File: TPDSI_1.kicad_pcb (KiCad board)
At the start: 2 copper layers, 83.8 x 61 mm, 63 parts, among them J1 Conn_01x02_Male, J2 Conn_01x02_Male, J3 Conn_01x10_Male, J4 Conn_01x04_Male, J5 Conn_01x04_Male, J6 Conn_01x06_Male, J7 Screw_Terminal_01x02, Q1 Q_NPN_BCE, Q2 Q_NPN_BCE, SW1 SW_Push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

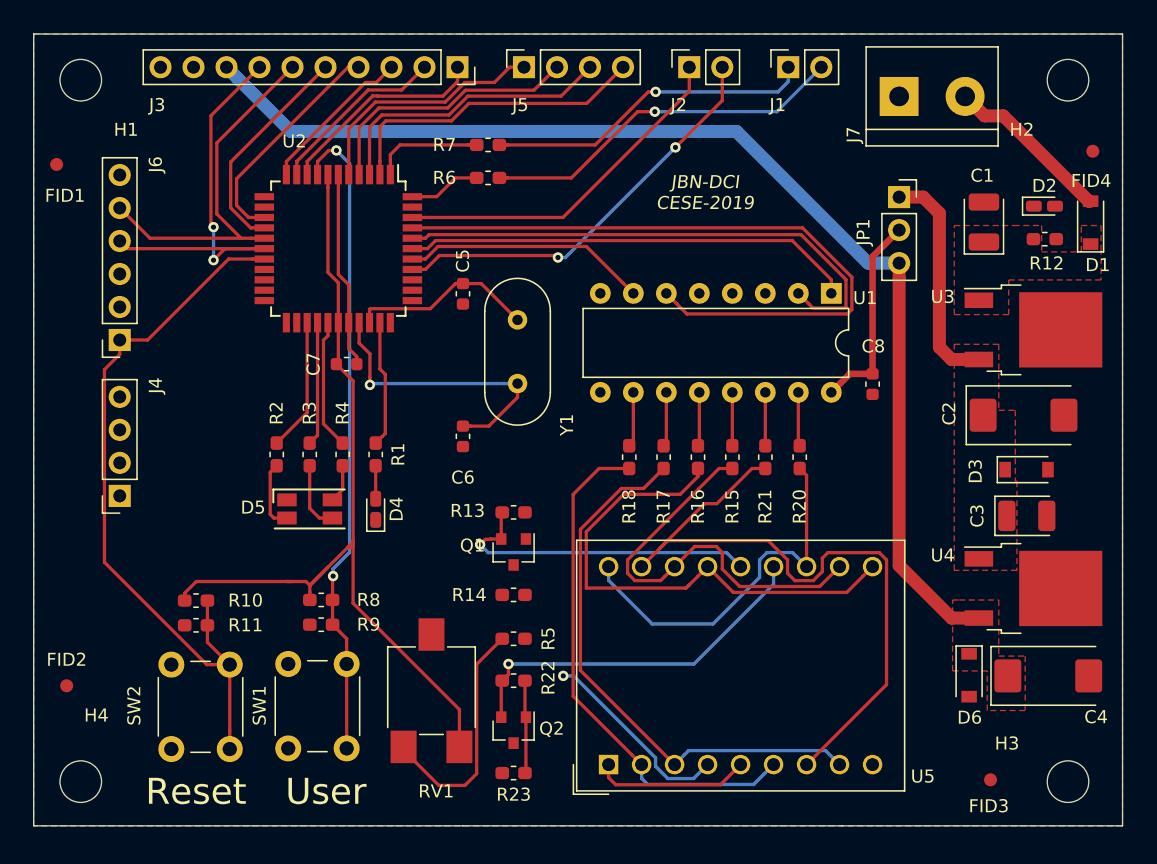
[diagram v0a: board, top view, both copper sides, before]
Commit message: Se agrega terminación de ruteo, con poligono de vcc y planos en top y bottom de gnd, pendiente realizar vías entre planos gnd, agregar datasheet y numeros de parte , insertar 3modelos  3D faltantes
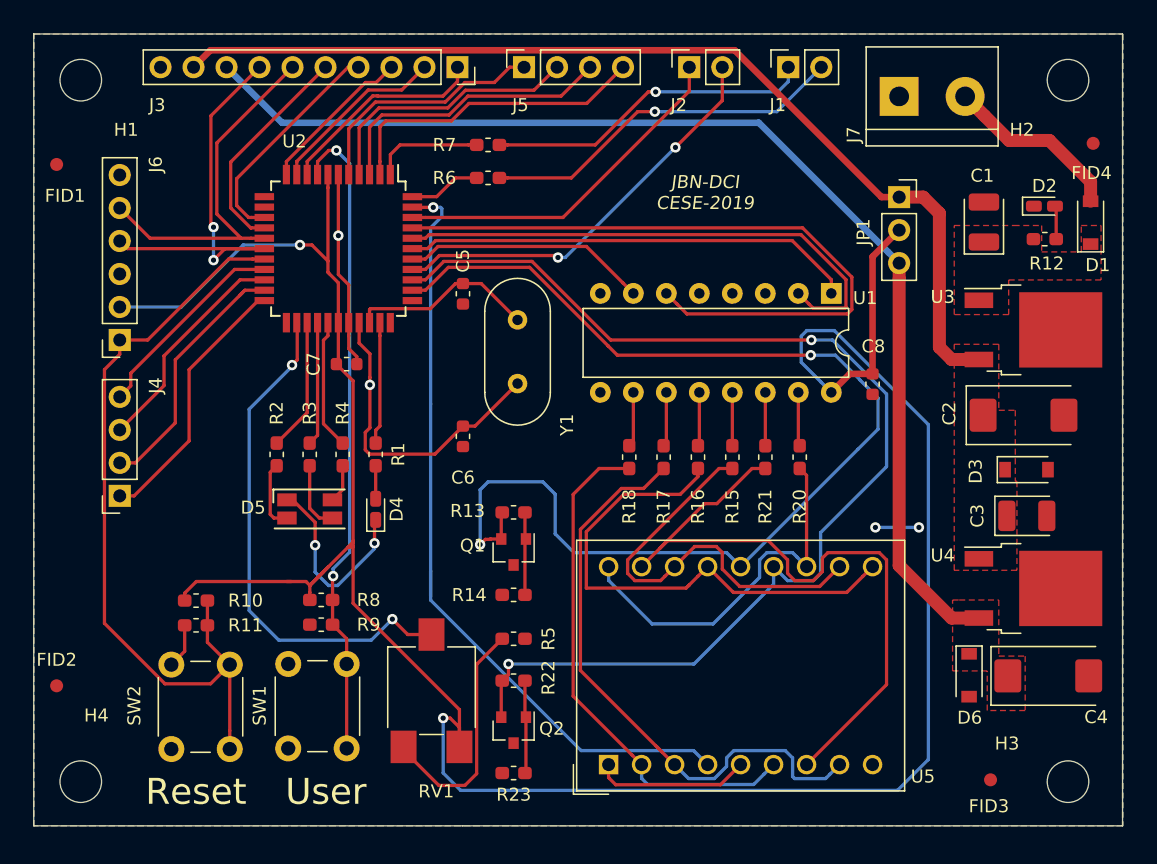
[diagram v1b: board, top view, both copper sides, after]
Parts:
- moved FID2 0.78 mm to (109.3, 112.3)
- moved FID4 0.61 mm to (189.1, 70.5)
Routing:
- net VDD: track 85.4 -> 194.2 mm, vias 0 -> 2
- net /Display/DIG1_CA: track 24.6 -> 91.0 mm, vias 1 -> 2
- net /Display/DIG2_CA: track 28.6 -> 90.2 mm, vias 1 -> 2
- net +5V: track 17.4 -> 76.9 mm
- net /Display/DP1: track 15.2 -> 61.3 mm
- net /POTENCIOMETRO: track 1.35 -> 41.4 mm, vias 0 -> 2
- net GND: track 15.2 -> 37.2 mm, vias 0 -> 5
- net /AN3: track 0.00 -> 20.6 mm
- net /AN2: track 0.00 -> 19.8 mm
- net /AN1: track 0.00 -> 17.3 mm
- net /AN0: track 0.00 -> 15.8 mm
- net Net-(Q1-Pad1): track 0.00 -> 6.41 mm
- net /Microcontroller/MCLR_VPP: track 56.4 -> 60.3 mm
- net /Display/c: track 43.0 -> 46.5 mm
- net Net-(D2-Pad2): track 0.00 -> 2.58 mm
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- added copper zone on B.Cu, net GND
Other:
- board text added: "*Capas 2 *Ancho de pista 0.254 mm *Clearence 0.254 mm keep out circular *Diametro via 0.8mm *Tdro via 0.4mm *Clearence planos 0.5 mm"
- board text removed: "*Capas 2 *Ancho de pista 0.254 mm *Clearence 0.254 mm keep out circular *Diametro via 0.8mm *Tdro via 0.4mm"

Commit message: Se agregan modelos 3D . Stp
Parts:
- moved J7 5.33 mm to (179.5, 66.9), turned to 180 degrees
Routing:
- net /9V0: track 13.9 -> 18.7 mm
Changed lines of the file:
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@@
   )
   (setup
-    (last_trace_width 0.254)
+    (last_trace_width 1)
     (user_trace_width 0.508)
     (user_trace_width 1)
@@
     (diff_pair_gap 0.25)
   )
+  (module TerminalBlock:TerminalBlock_bornier-2_P5.08mm (layer F.Cu)
+    (at 179.5272 66.898 180)
+    (descr "simple 2-pin terminal block, pitch 5.08mm, revamped version of bornier2")
+    (tags "terminal block bornier2")
+    (fp_text reference J7 (at -3.505 2.952 90) (layer F.SilkS)
+      (effects (font (size 1 1) (thickness 0.15)))
+    )
+    (fp_text value Screw_Terminal_01x02 (at 2.54 5.08) (layer F.Fab)
+      (effects (font (size 1 1) (thickness 0.15)))
+    )
+    (fp_line (start 7.79 4) (end -2.71 4) (layer F.CrtYd) (width 0.05))
+    (fp_line (start 7.79 4) (end 7.79 -4) (layer F.CrtYd) (width 0.05))
+    (fp_line (start -2.71 -4) (end -2.71 4) (layer F.CrtYd) (width 0.05))
+    (fp_line (start -2.71 -4) (end 7.79 -4) (layer F.CrtYd) (width 0.05))
+    (fp_line (start -2.54 3.81) (end 7.62 3.81) (layer F.SilkS) (width 0.12))
+    (fp_line (start -2.54 -3.81) (end -2.54 3.81) (layer F.SilkS) (width 0.12))
+    (fp_line (start 7.62 -3.81) (end -2.54 -3.81) (layer F.SilkS) (width 0.12))
+    (fp_line (start 7.62 3.81) (end 7.62 -3.81) (layer F.SilkS) (width 0.12))
+    (fp_line (start 7.62 2.54) (end -2.54 2.54) (layer F.SilkS) (width 0.12))
+    (fp_line (start 7.54 -3.75) (end -2.46 -3.75) (layer F.Fab) (width 0.1))
+    (fp_line (start 7.54 3.75) (end 7.54 -3.75) (layer F.Fab) (width 0.1))
+    (fp_line (start -2.46 3.75) (end 7.54 3.75) (layer F.Fab) (width 0.1))
+    (fp_line (start -2.46 -3.75) (end -2.46 3.75) (layer F.Fab) (width 0.1))
+    (fp_line (start -2.41 2.55) (end 7.49 2.55) (layer F.Fab) (width 0.1))
+    (fp_text user %R (at 2.54 0) (layer F.Fab)
+      (effects (font (size 1 1) (thickness 0.15)))
+    )
+    (pad 2 thru_hole circle (at 5.08 0 180) (size 3 3) (drill 1.52) (layers *.Cu *.Mask)
+      (net 8 /9V0))
+    (pad 1 thru_hole rect (at 0 0 180) (size 3 3) (drill 1.52) (layers *.Cu *.Mask)
+      (net 1 GND))
+    (model ${KISYS3DMOD}/TerminalBlock.3dshapes/TerminalBlock_bornier-2_P5.08mm.wrl
+      (offset (xyz 2.539999961853027 0 0))
+      (scale (xyz 1 1 1))
+      (rotate (xyz 0 0 0))
+    )
+    (model "${KIPRJMOD}/User Library-DG301-5_0-2P12/User Library-DG301-5_0-2P12.STEP"
+      (at (xyz 0 0 0))
+      (scale (xyz 1 1 1))
+      (rotate (xyz 0 0 0))
+    )
+  )
   (module Display_7Segment:DA56-11CGKWA (layer F.Cu)
     (at 151.827 118.335 90)
@@
       (rotate (xyz 0 0 0))
     )
-  )
-  (module TerminalBlock:TerminalBlock_bornier-2_P5.08mm (layer F.Cu)
-    (at 174.193 66.898)
-    (descr "simple 2-pin terminal block, pitch 5.08mm, revamped version of bornier2")
-    (tags "terminal block bornier2")
-    (fp_text reference J7 (at -3.505 2.952 90) (layer F.SilkS)
-      (effects (font (size 1 1) (thickness 0.15)))
-    )
-    (fp_text value Screw_Terminal_01x02 (at 2.54 5.08) (layer F.Fab)
-      (effects (font (size 1 1) (thickness 0.15)))
-    )
-    (fp_line (start 7.79 4) (end -2.71 4) (layer F.CrtYd) (width 0.05))
-    (fp_line (start 7.79 4) (end 7.79 -4) (layer F.CrtYd) (width 0.05))
-    (fp_line (start -2.71 -4) (end -2.71 4) (layer F.CrtYd) (width 0.05))
-    (fp_line (start -2.71 -4) (end 7.79 -4) (layer F.CrtYd) (width 0.05))
-    (fp_line (start -2.54 3.81) (end 7.62 3.81) (layer F.SilkS) (width 0.12))
-    (fp_line (start -2.54 -3.81) (end -2.54 3.81) (layer F.SilkS) (width 0.12))
-    (fp_line (start 7.62 -3.81) (end -2.54 -3.81) (layer F.SilkS) (width 0.12))
-    (fp_line (start 7.62 3.81) (end 7.62 -3.81) (layer F.SilkS) (width 0.12))
-    (fp_line (start 7.62 2.54) (end -2.54 2.54) (layer F.SilkS) (width 0.12))
-    (fp_line (start 7.54 -3.75) (end -2.46 -3.75) (layer F.Fab) (width 0.1))
-    (fp_line (start 7.54 3.75) (end 7.54 -3.75) (layer F.Fab) (width 0.1))
-    (fp_line (start -2.46 3.75) (end 7.54 3.75) (layer F.Fab) (width 0.1))
-    (fp_line (start -2.46 -3.75) (end -2.46 3.75) (layer F.Fab) (width 0.1))
-    (fp_line (start -2.41 2.55) (end 7.49 2.55) (layer F.Fab) (width 0.1))
-    (fp_text user %R (at 2.54 0) (layer F.Fab)
-      (effects (font (size 1 1) (thickness 0.15)))
-    )
-    (pad 2 thru_hole circle (at 5.08 0) (size 3 3) (drill 1.52) (layers *.Cu *.Mask)
-      (net 8 /9V0))
-    (pad 1 thru_hole rect (at 0 0) (size 3 3) (drill 1.52) (layers *.Cu *.Mask)
-      (net 1 GND))
-    (model ${KISYS3DMOD}/TerminalBlock.3dshapes/TerminalBlock_bornier-2_P5.08mm.wrl
-      (offset (xyz 2.539999961853027 0 0))
-      (scale (xyz 1 1 1))
-      (rotate (xyz 0 0 0))
+    (model "${KIPRJMOD}/User Library-CA6V-SMD/User Library-CA6V-SMD.STEP"
+      (offset (xyz -3 3.25 0.3))
+      (scale (xyz 1 1 1))
+      (rotate (xyz 90 180 -90))
     )
   )
@@
       (scale (xyz 1 1 1))
       (rotate (xyz 0 0 0))
+    )
+    (model "${KIPRJMOD}/User Library-led_1210/User Library-led_1210.STEP"
+      (at (xyz 0 0 0))
+      (scale (xyz 1 1 1))
+      (rotate (xyz 0 0 90))
     )
   )
@@
   (segment (start 118.9236 83.108) (end 123.698 78.3336) (width 0.254) (layer B.Cu) (net 7))
   (segment (start 114.193 83.108) (end 118.9236 83.108) (width 0.254) (layer B.Cu) (net 7))
-  (segment (start 188.933 74.965) (end 188.933 73.4646) (width 1) (layer F.Cu) (net 8))
-  (segment (start 180.772999 68.397999) (end 179.273 66.898) (width 1) (layer F.Cu) (net 8))
-  (segment (start 182.663001 70.288001) (end 180.772999 68.397999) (width 1) (layer F.Cu) (net 8))
-  (segment (start 185.756401 70.288001) (end 182.663001 70.288001) (width 1) (layer F.Cu) (net 8))
-  (segment (start 188.933 73.4646) (end 185.756401 70.288001) (width 1) (layer F.Cu) (net 8))
+  (segment (start 175.947199 68.397999) (end 174.4472 66.898) (width 1) (layer F.Cu) (net 8))
+  (segment (start 179.559601 72.010401) (end 175.947199 68.397999) (width 1) (layer F.Cu) (net 8))
+  (segment (start 187.428401 72.010401) (end 179.559601 72.010401) (width 1) (layer F.Cu) (net 8))
+  (segment (start 188.933 73.515) (end 187.428401 72.010401) (width 1) (layer F.Cu) (net 8))
+  (segment (start 188.933 74.965) (end 188.933 73.515) (width 1) (layer F.Cu) (net 8))
   (segment (start 186.283 75.4375) (end 186.1905 75.345) (width 0.254) (layer F.Cu) (net 9))
   (segment (start 186.283 77.885) (end 186.283 75.4375) (width 0.254) (layer F.Cu) (net 9))

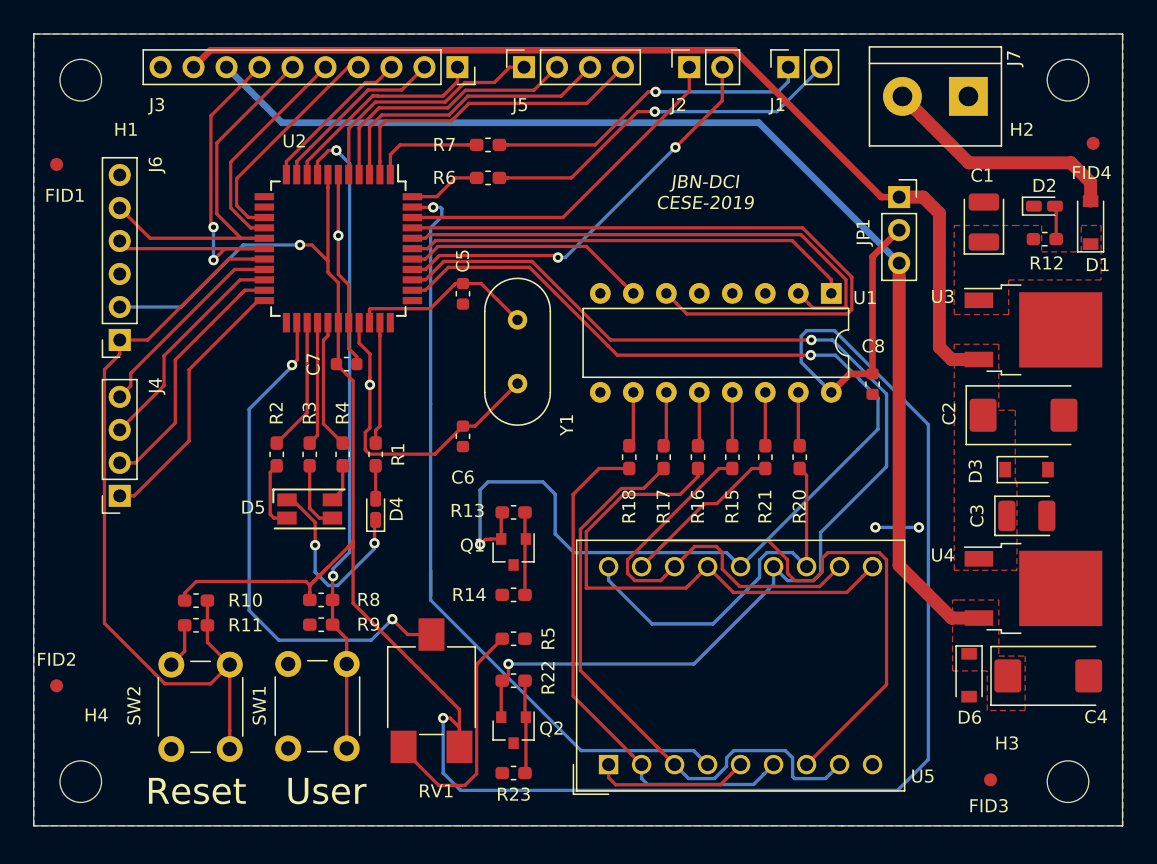
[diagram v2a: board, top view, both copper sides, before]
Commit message: PCB: Se agrega via stitching entre planos, Rev estable
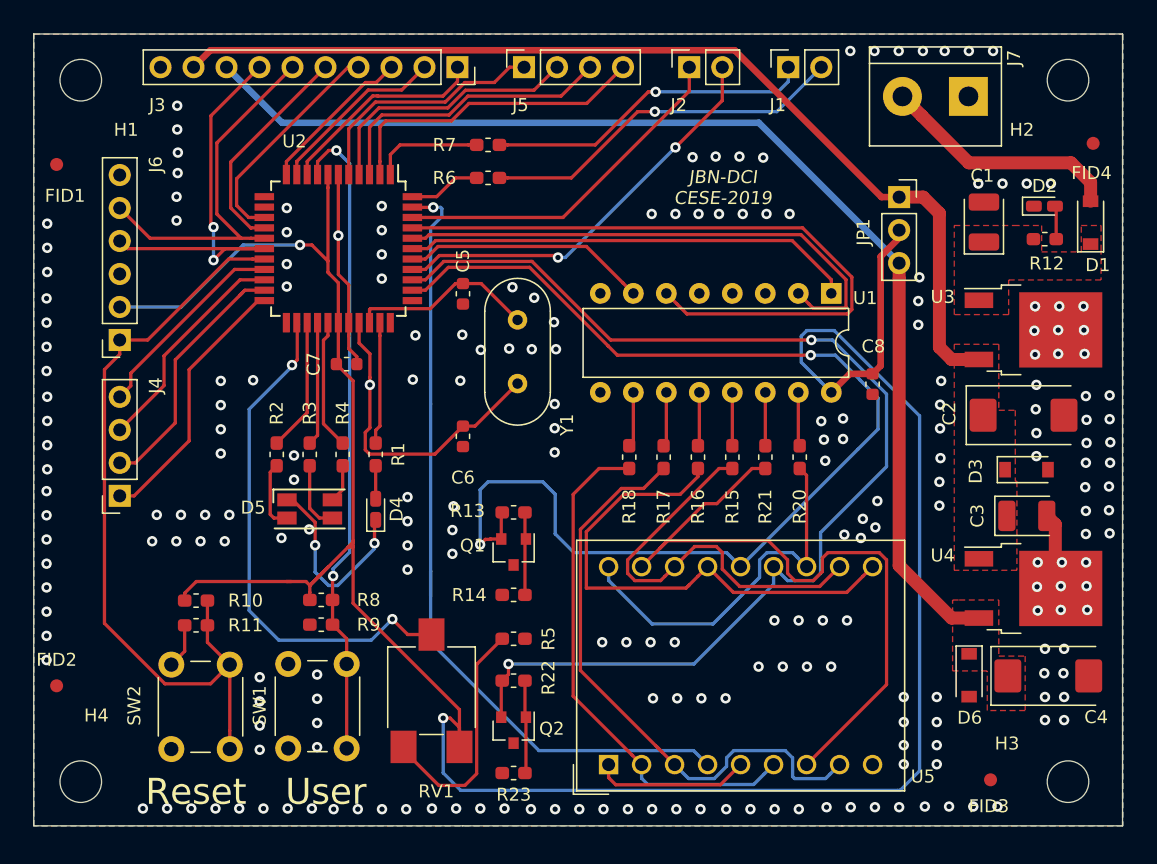
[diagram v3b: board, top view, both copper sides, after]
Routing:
- net /Display/DP1: track 61.3 -> 63.2 mm
- net GND: track 37.2 -> 37.8 mm, vias 5 -> 224
- net (no net): vias 0 -> 3
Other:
- board text added: "*Colocar tented a las vias en la fabricación *Terminación HALS"

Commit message: Se agregan cosas obligatorias por norma y algunas sugerencias por el docente
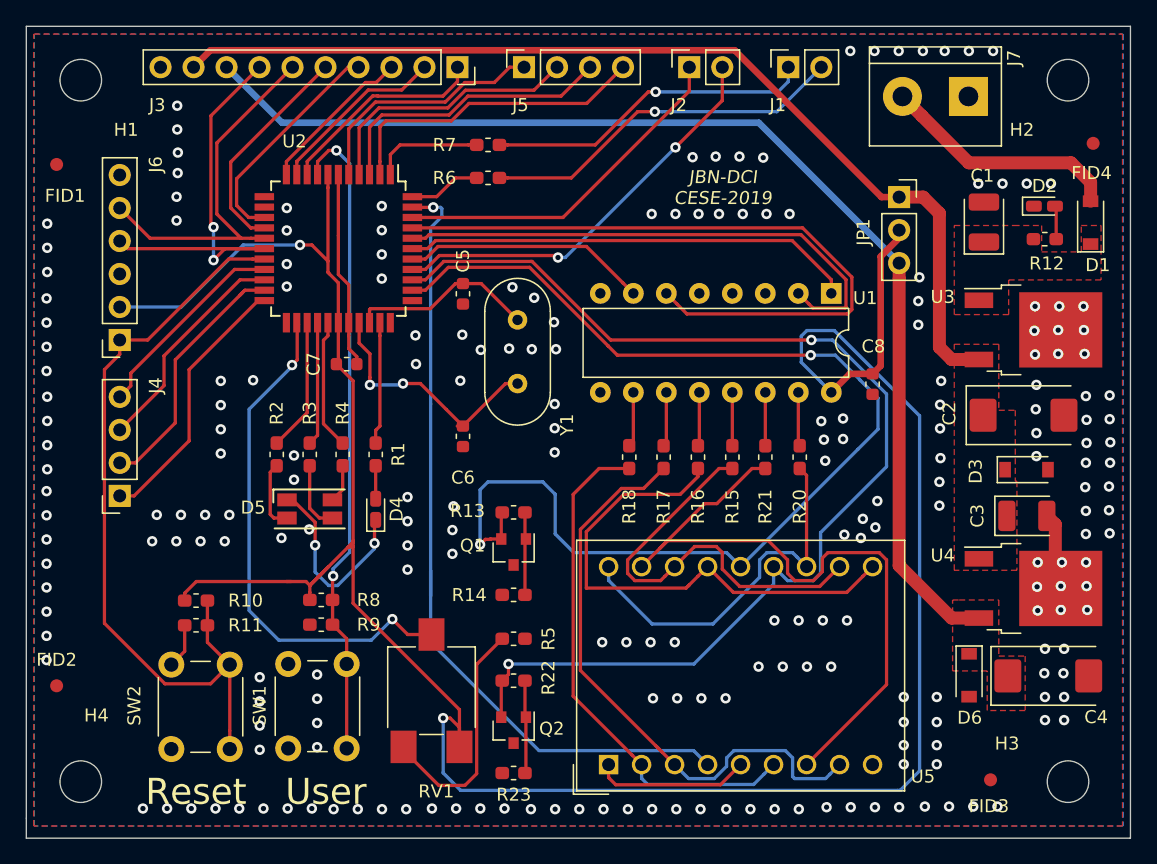
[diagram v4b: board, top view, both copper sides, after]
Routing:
- net Net-(C6-Pad2): track 24.5 -> 19.7 mm, vias 1 -> 2
- net GND: vias 224 -> 223
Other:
- board size 83.8 x 61 mm -> 85 x 62.5 mm
- board text added: "*Colocar tented a las vias en la fabricación *Terminación HASL *Fabricante criterios dimención : https://www.colcircuitos.com/wp-content/uploads/2017/08/REQUERIMIENTOS-MINIMOS-FE-2017.pdf"
- board text added: "*Grilla borde pcb 0.5 mm"
- board text added: "INDUSTRIA COLOMBIANA"
- board text removed: "*Colocar tented a las vias en la fabricación *Terminación HALS"

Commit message: se agrega serigrafía a conectores, pin header, industria colombiana
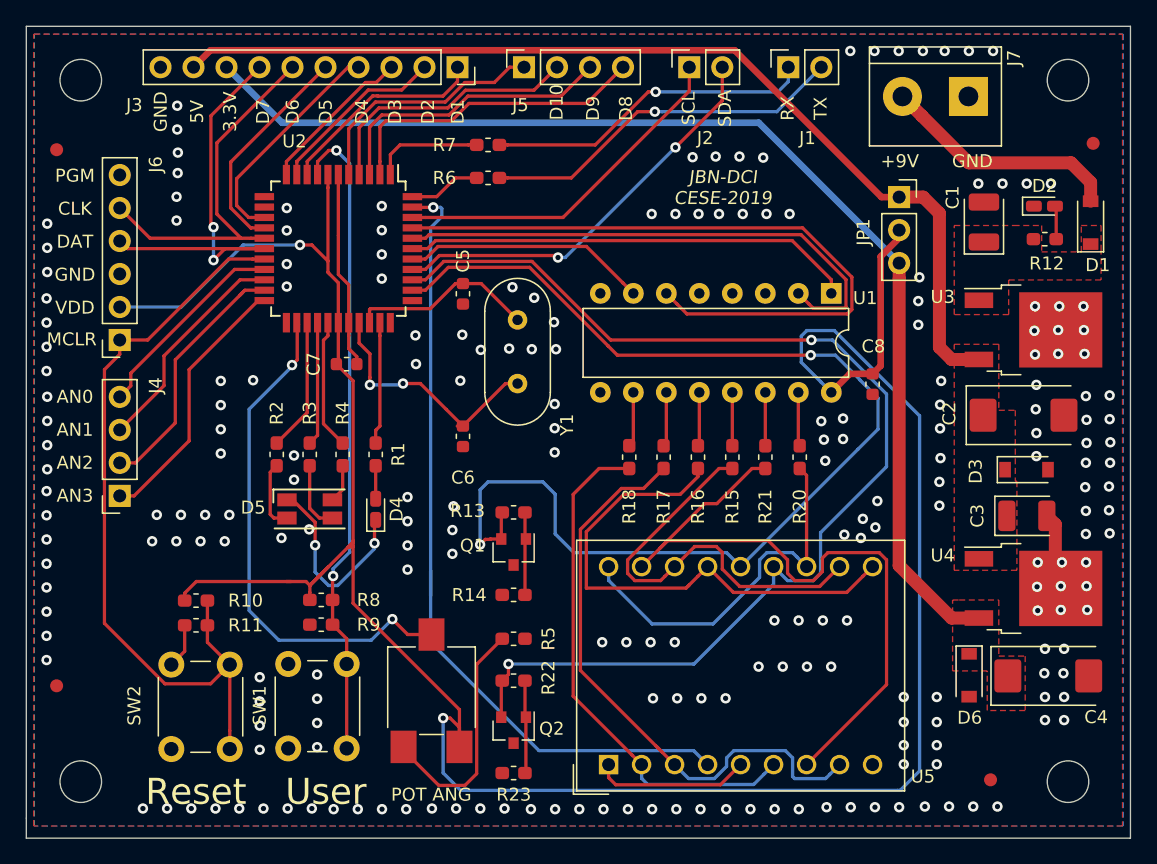
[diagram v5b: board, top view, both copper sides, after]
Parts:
- moved FID1 1.14 mm to (109.3, 71.0)
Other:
- board text added: "+9V"
- board text added: "3.3V"
- board text added: "5V"
- board text added: "AN0"
- board text added: "AN1"
- board text added: "AN2"
- board text added: "AN3"
- board text added: "CLK"
- board text added: "D1"
- board text added: "D10"
- board text added: "D2"
- board text added: "D3"
- board text added: "D4"
- board text added: "D5"
- board text added: "D6"
- board text added: "D7"
- board text added: "D8"
- board text added: "D9"
- board text added: "DAT"
- board text added: "GND"
- board text added: "MCLR"
- board text added: "PGM"
- board text added: "POT ANG"
- board text added: "RX"
- board text added: "SCL"
- board text added: "SDA"
- board text added: "TX"
- board text added: "VDD"
